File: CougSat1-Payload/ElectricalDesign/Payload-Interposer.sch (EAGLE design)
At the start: 59 parts, among them J1 CougSat Card, J3 Interposer, J5 Germination Chamber, Q1 CSD25402Q3A, Q2 CSD25402Q3A, U1 TXS0102DQM, U14 TPS61220, U15 TPS73250, U2 TXS0102DQM, U3 TXS0102DQM, U4 BME280, U5 TLC59116F, U6 TXS0102DQM

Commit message: made more changes required
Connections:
- net I2C_SCL_GERM: now also U6.A1
- net I2C_SDA_GERM: now also U6.A2
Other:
- note added: "CAD Note: Bulk Capacitor"
- note added: "Page 1: Block Diagram Page 2: Power Rails Page 3: Interposer Page 4: Voltage Regulator Page 5: Chamber Page 6: Mechanical"
- note added: "Page 3"
- note added: "Page 4"
- note removed: "Page 1: Block Diagram Page 2: Power Rails"
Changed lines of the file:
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@@
 <setting verticaltext="up"/>
 </settings>
-<grid distance="0.1" unitdist="inch" unit="inch" style="lines" multiple="1" display="no" altdistance="0.01" altunitdist="inch" altunit="inch"/>
+<grid distance="0.1" unitdist="inch" unit="inch" style="lines" multiple="1" display="yes" altdistance="0.01" altunitdist="inch" altunit="inch"/>
 <layers>
 <layer number="1" name="Top" color="4" fill="1" visible="no" active="no"/>
@@
 <wire x1="137.16" y1="25.4" x2="0" y2="25.4" width="0.254" layer="94"/>
 <text x="1.27" y="24.13" size="1.778" layer="97" align="top-left">Page 1: Block Diagram
-Page 2: Power Rails</text>
+Page 2: Power Rails
+Page 3: Interposer
+Page 4: Voltage Regulator
+Page 5: Chamber
+Page 6: Mechanical</text>
 <text x="101.6" y="91.694" size="1.778" layer="97" align="bottom-center">SPI</text>
 <text x="33.02" y="144.78" size="3.81" layer="94" align="center">Heater</text>
@@
 <wire x1="193.04" y1="76.2" x2="167.64" y2="76.2" width="0.254" layer="94"/>
 <wire x1="167.64" y1="76.2" x2="167.64" y2="116.84" width="0.254" layer="94"/>
-<text x="180.64" y="97.58" size="3.81" layer="94" rot="MR0" align="center">Interposer</text>
+<text x="180.34" y="96.52" size="3.81" layer="94" rot="MR0" align="center">Interposer</text>
 <text x="127" y="96.52" size="3.81" layer="94" align="center">Germination
 Chamber
@@
 <wire x1="83.82" y1="104.14" x2="86.36" y2="106.68" width="0.254" layer="97"/>
 <wire x1="83.82" y1="104.14" x2="86.36" y2="101.6" width="0.254" layer="97"/>
+<text x="180.34" y="88.9" size="1.778" layer="97" align="bottom-center">Page 3</text>
+<text x="127" y="83.82" size="1.778" layer="97" align="bottom-center">Page 4</text>
 </plain>
 <instances>
@@
 <text x="55.88" y="88.9" size="1.27" layer="97" align="center-left">  4A3&gt; </text>
 <text x="88.9" y="160.02" size="1.778" layer="97" align="center-right"> &gt;4B2 </text>
+<text x="180.34" y="99.06" size="1.778" layer="97">CAD Note:
+Bulk Capacitor</text>
+<wire x1="177.8" y1="104.14" x2="177.8" y2="81.28" width="0.1524" layer="97" style="shortdash"/>
+<wire x1="177.8" y1="81.28" x2="198.12" y2="81.28" width="0.1524" layer="97" style="shortdash"/>
+<wire x1="198.12" y1="81.28" x2="198.12" y2="104.14" width="0.1524" layer="97" style="shortdash"/>
+<wire x1="198.12" y1="104.14" x2="177.8" y2="104.14" width="0.1524" layer="97" style="shortdash"/>
 </plain>
 <instances>
@@
 <pinref part="R3" gate="G$1" pin="1"/>
 <pinref part="U4" gate="G$1" pin="SDI"/>
-<wire x1="73.66" y1="160.02" x2="73.66" y2="109.22" width="0.1524" layer="91"/>
+<wire x1="73.66" y1="160.02" x2="73.66" y2="134.62" width="0.1524" layer="91"/>
+<wire x1="73.66" y1="134.62" x2="73.66" y2="109.22" width="0.1524" layer="91"/>
 <wire x1="66.04" y1="160.02" x2="73.66" y2="160.02" width="0.1524" layer="91"/>
 <junction x="73.66" y="109.22"/>
@@
 <wire x1="116.84" y1="63.5" x2="73.66" y2="63.5" width="0.1524" layer="91"/>
 <junction x="73.66" y="63.5"/>
+<pinref part="U6" gate="G$1" pin="A2"/>
+<wire x1="83.82" y1="134.62" x2="73.66" y2="134.62" width="0.1524" layer="91"/>
+<junction x="73.66" y="134.62"/>
 </segment>
 </net>
@@
 <wire x1="76.2" y1="106.68" x2="76.2" y2="66.04" width="0.1524" layer="91"/>
 <wire x1="76.2" y1="66.04" x2="76.2" y2="20.32" width="0.1524" layer="91"/>
-<wire x1="76.2" y1="106.68" x2="76.2" y2="165.1" width="0.1524" layer="91"/>
+<wire x1="76.2" y1="106.68" x2="76.2" y2="139.7" width="0.1524" layer="91"/>
+<wire x1="76.2" y1="139.7" x2="76.2" y2="165.1" width="0.1524" layer="91"/>
 <wire x1="76.2" y1="165.1" x2="66.04" y2="165.1" width="0.1524" layer="91"/>
 <label x="27.94" y="106.68" size="1.778" layer="95"/>
@@
 <wire x1="116.84" y1="66.04" x2="76.2" y2="66.04" width="0.1524" layer="91"/>
 <junction x="76.2" y="66.04"/>
-</segment>
-</net>
+<pinref part="U6" gate="G$1" pin="A1"/>
+<wire x1="83.82" y1="139.7" x2="76.2" y2="139.7" width="0.1524" layer="91"/>
+<junction x="76.2" y="139.7"/>
+</segment>
+</net>

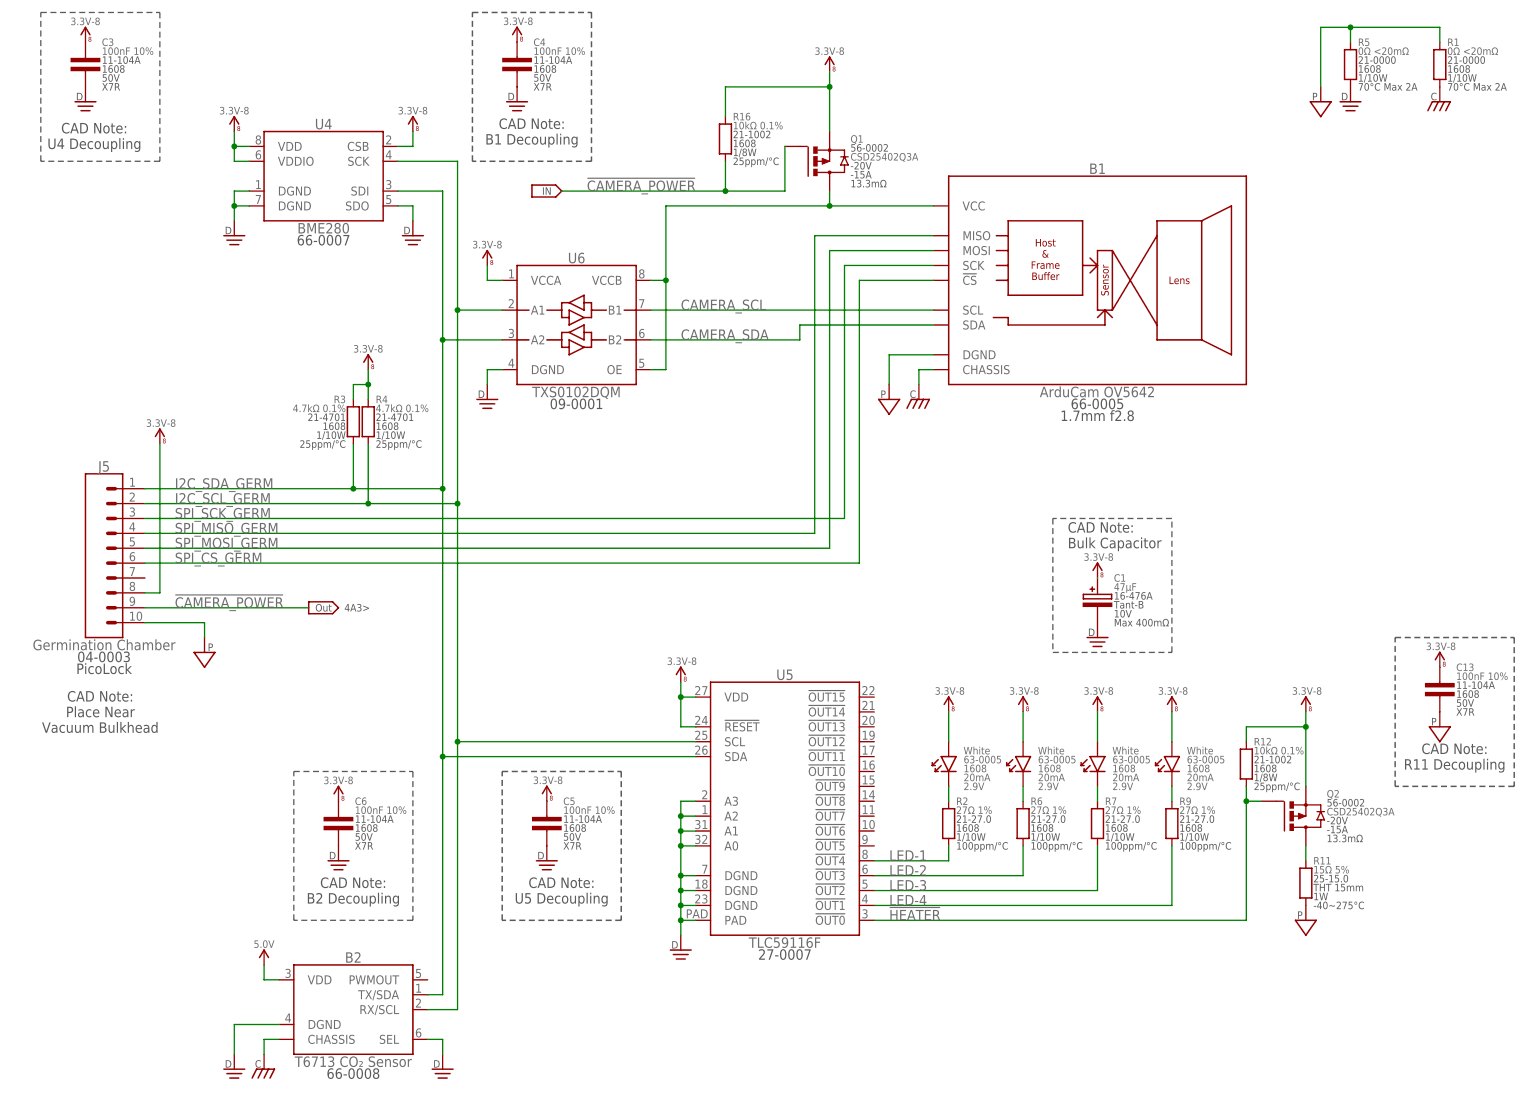
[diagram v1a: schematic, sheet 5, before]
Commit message: Created board, placed/arranged some components
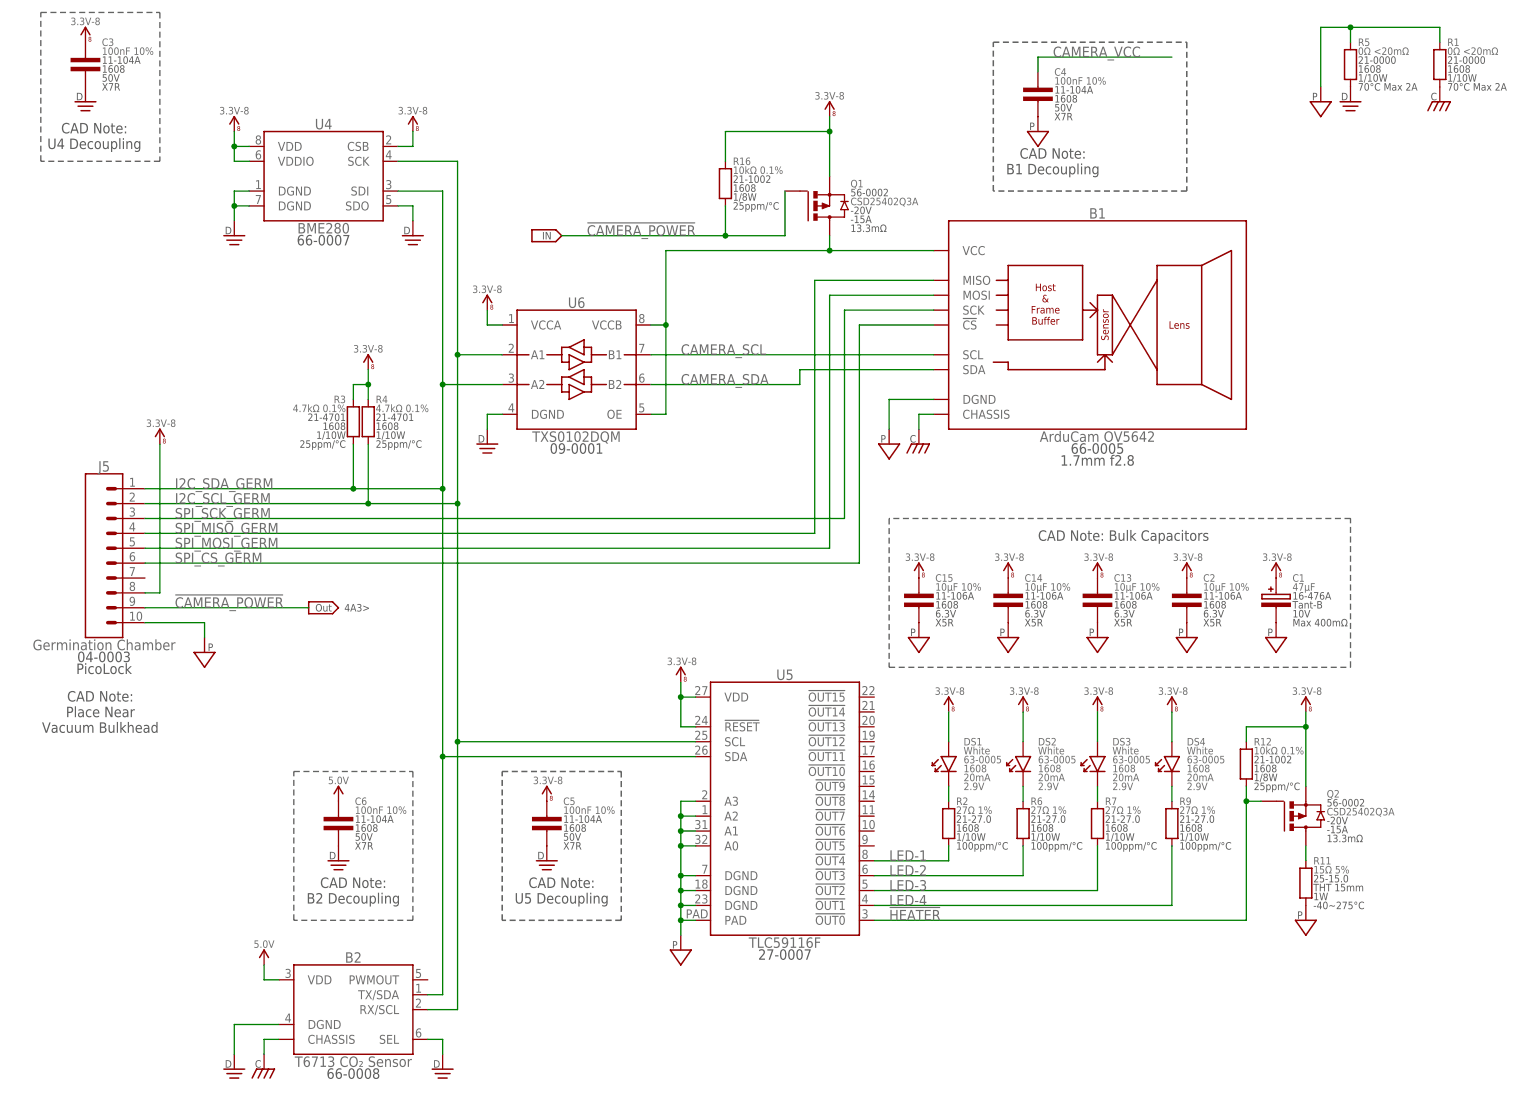
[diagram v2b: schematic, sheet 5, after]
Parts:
- added C14, C15, C2: 10µF 10%, CougsInSpace-Capacitors:CAP-V-10UF-1608
- C13: value 100nF 10% -> 10µF 10%; device CougsInSpace-Capacitors:CAP-V-100NF-1608 -> CougsInSpace-Capacitors:CAP-V-10UF-1608
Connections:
- net 3.3V_8: now also C14.1, C15.1, C2.1; no longer C4.1, C6.1
- net 5.0V: now also C6.1
- net CAMERA_VCC: now also C4.1
- net DGND: no longer C1.C, C4.2, U5.A0, U5.A1, U5.A2, U5.A3, U5.DGND@1, U5.DGND@2, U5.DGND@3, U5.PAD
- net PGND: now also C1.C, C14.2, C15.2, C2.2, C4.2, U5.A0, U5.A1, U5.A2, U5.A3, U5.DGND@1, U5.DGND@2, U5.DGND@3, U5.PAD
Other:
- note added: "CAD Note: Bulk Capacitors"
- note removed: "CAD Note: Bulk Capacitor"
- note removed: "CAD Note: R11 Decoupling"
- moved on the sheet: B1, C1, C13, C4, J1MECH-BOTTOM, J1MECH-TOP, Q1, R16, U6

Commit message: Worked on layout
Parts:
- removed R11: 15Ω 5%, CougsInSpace-Resistors:RES-V-15R-THT-15MM
- added J2, J4: Heater, CougsInSpace-Connectors:1X01-THT-1.5
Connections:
- net HEATER_SOURCE: now also J2.1; no longer R11.2
- net PGND: now also J4.1; no longer R11.1
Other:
- moved on the sheet: C1, C13, C14, C15, C2, C5, DS1, DS2, DS3, DS4, Q2, R12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
